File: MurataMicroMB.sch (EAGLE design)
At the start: 47 parts, among them CON1 C-2395.MurataMicroSD, CON3 CON_MIL_10_ARM, CON4 C-2395.microSD, IC1 74LVC1G00DBV, IC2 IC_DCDC_LM27313, IC3 IC_LPC11U3XQFN33, IC4 IC_LDO_XX1117_4, Q1 CLOCK_CRYSTAL_4_3225, SW1 SW_TACTSW_2PP8073, SW2 SW_TACTSW_2PP8073, SW3 SW_TACTSW_2PP8073, X1 TSW-102-02-S-S

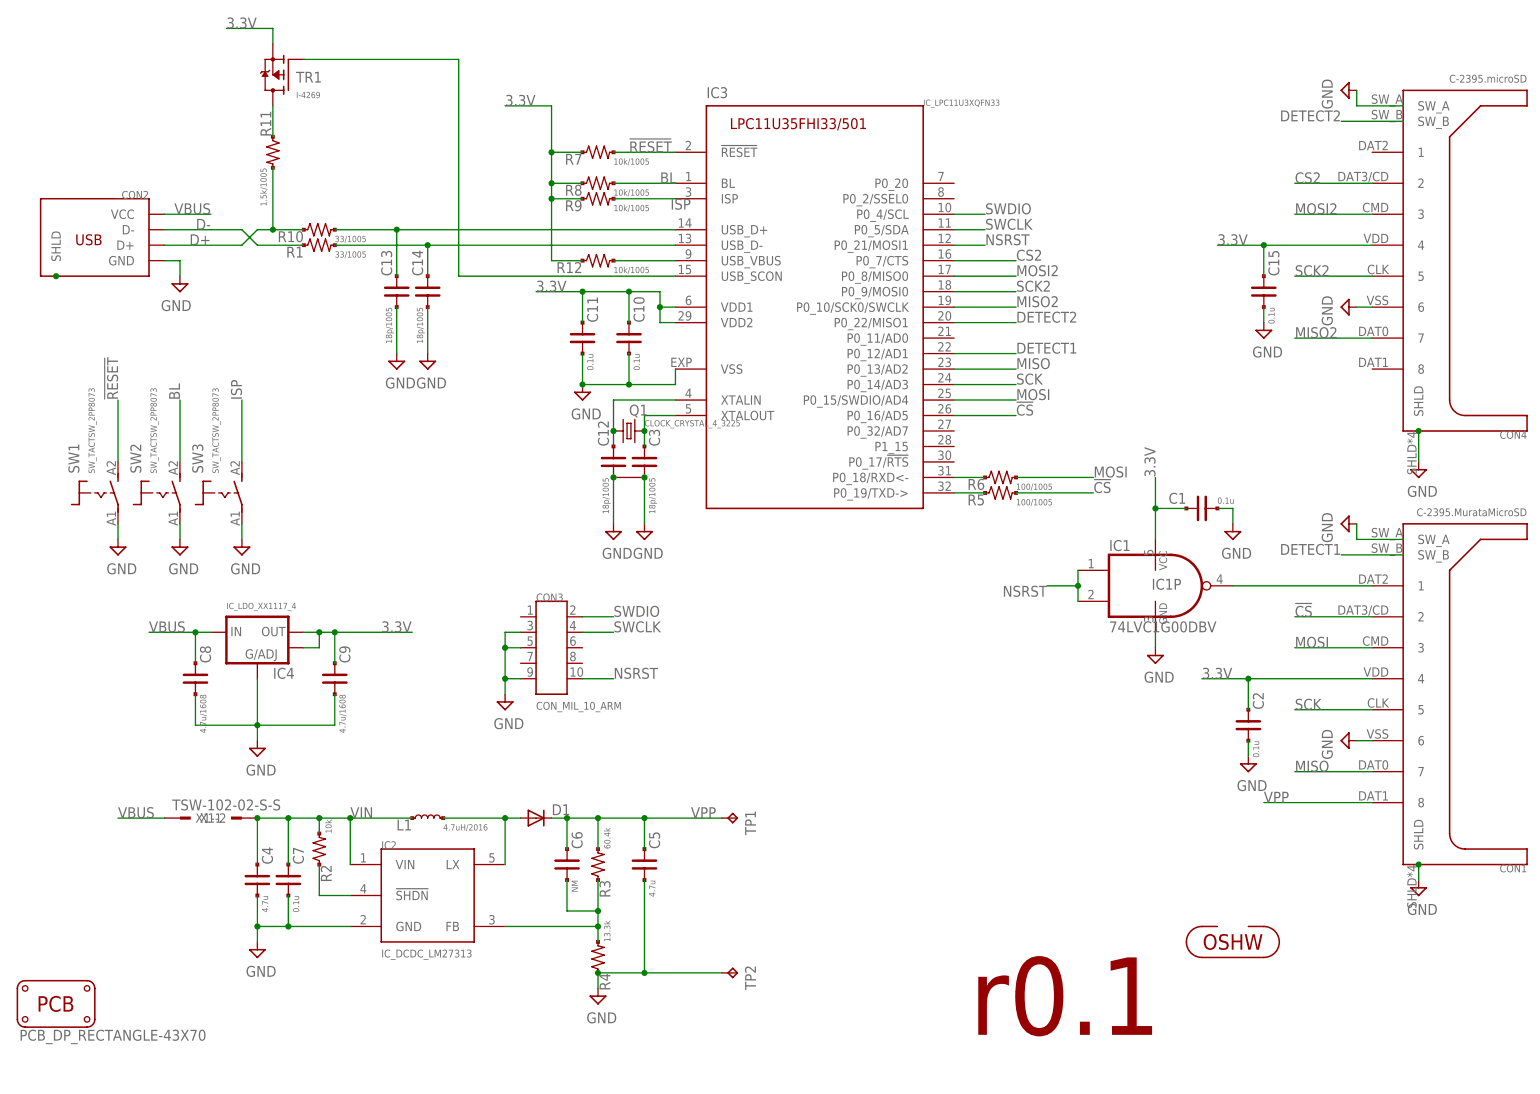
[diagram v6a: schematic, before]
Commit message: [ MB ] add LED1/R13/R14
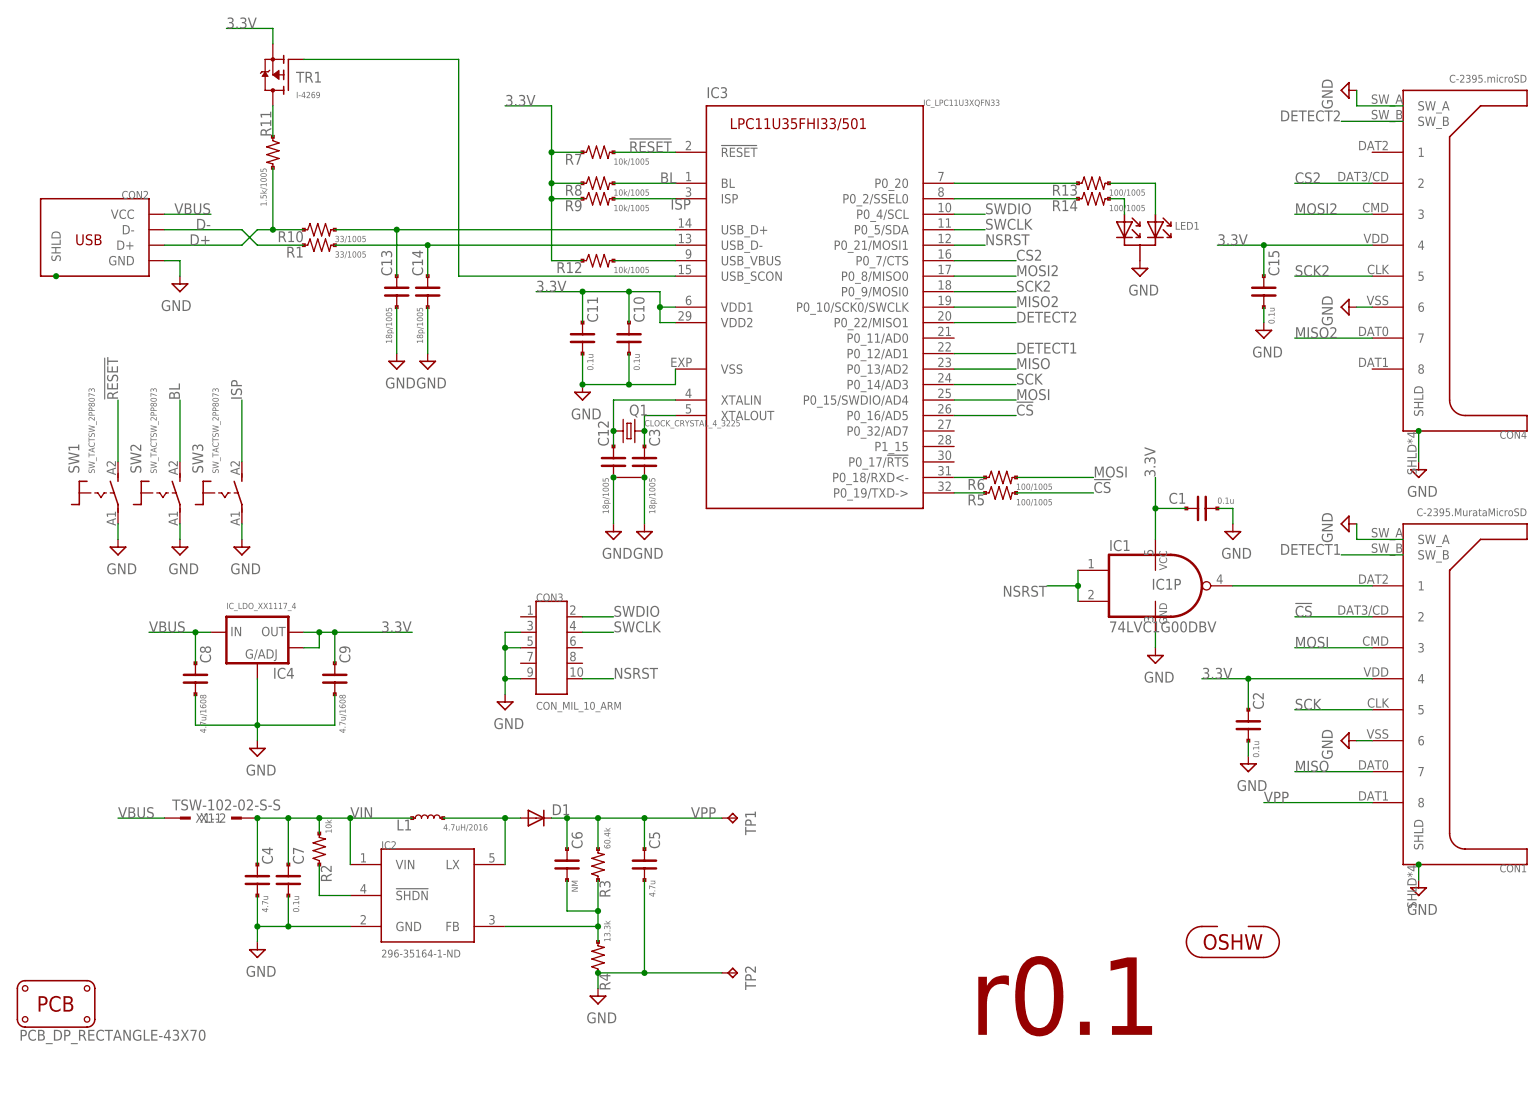
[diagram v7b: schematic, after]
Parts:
- added LED1: (no value), mylib:LED_1SEG_A2K1
- added R13, R14: 100/1005, mylib:R_US_PAD_PAD_1005
- IC2: value IC_DCDC_LM27313 -> 296-35164-1-ND
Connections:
- new net N$1: IC3.P0_2/SSEL0, R14.1
- new net N$14: IC3.P0_20, R13.1
- new net N$15: LED1.A2, R13.2
- new net N$16: LED1.A1, R14.2
- net GND: now also LED1.K1
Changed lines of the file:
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@@
 <part name="SUPPLY8" library="mylib" deviceset="GND" device=""/>
 <part name="L1" library="mylib" deviceset="INDUCTOR" device="_2016" value="4.7uH/2016"/>
-<part name="IC2" library="mylib" deviceset="IC_DCDC_LM27313" device=""/>
+<part name="IC2" library="mylib" deviceset="IC_DCDC_LM27313" device="" value="296-35164-1-ND"/>
 <part name="D1" library="mylib" deviceset="DIODE_SMALL" device=""/>
 <part name="R2" library="mylib" deviceset="R_US_PAD_PAD" device="_1608" value="10k"/>
@@
 <part name="SUPPLY22" library="mylib" deviceset="GND" device=""/>
 <part name="SUPPLY23" library="mylib" deviceset="GND" device=""/>
+<part name="R13" library="mylib" deviceset="R_US_PAD_PAD" device="_1005" value="100/1005"/>
+<part name="R14" library="mylib" deviceset="R_US_PAD_PAD" device="_1005" value="100/1005"/>
+<part name="LED1" library="mylib" deviceset="LED_1SEG_A2K1" device=""/>
+<part name="SUPPLY24" library="mylib" deviceset="GND" device=""/>
 </parts>
 <sheets>
@@
 <instance part="SUPPLY22" gate="GND" x="223.52" y="160.02" rot="R270"/>
 <instance part="SUPPLY23" gate="GND" x="223.52" y="88.9" rot="R270"/>
+<instance part="R13" gate="G$1" x="182.88" y="144.78"/>
+<instance part="R14" gate="G$1" x="182.88" y="142.24"/>
+<instance part="LED1" gate="G$1" x="190.5" y="137.16"/>
+<instance part="SUPPLY24" gate="GND" x="190.5" y="129.54"/>
 </instances>
 <busses>
@@
 <wire x1="226.06" y1="88.9" x2="226.06" y2="86.36" width="0.1524" layer="91"/>
 <wire x1="226.06" y1="86.36" x2="233.68" y2="86.36" width="0.1524" layer="91"/>
+</segment>
+<segment>
+<pinref part="LED1" gate="G$1" pin="K1"/>
+<pinref part="SUPPLY24" gate="GND" pin="GND"/>
 </segment>
 </net>
@@
 </segment>
 </net>
+<net name="N$1" class="0">
+<segment>
+<pinref part="R14" gate="G$1" pin="1"/>
+<pinref part="IC3" gate="G$1" pin="P0_2/SSEL0"/>
+<wire x1="180.34" y1="142.24" x2="160.02" y2="142.24" width="0.1524" layer="91"/>
+</segment>
+</net>
+<net name="N$14" class="0">
+<segment>
+<pinref part="IC3" gate="G$1" pin="P0_20"/>
+<pinref part="R13" gate="G$1" pin="1"/>
+<wire x1="160.02" y1="144.78" x2="180.34" y2="144.78" width="0.1524" layer="91"/>
+</segment>
+</net>
+<net name="N$15" class="0">
+<segment>
+<pinref part="R13" gate="G$1" pin="2"/>
+<pinref part="LED1" gate="G$1" pin="A2"/>
+<wire x1="185.42" y1="144.78" x2="193.04" y2="144.78" width="0.1524" layer="91"/>
+<wire x1="193.04" y1="144.78" x2="193.04" y2="139.7" width="0.1524" layer="91"/>
+</segment>
+</net>
+<net name="N$16" class="0">
+<segment>
+<pinref part="R14" gate="G$1" pin="2"/>
+<pinref part="LED1" gate="G$1" pin="A1"/>
+<wire x1="185.42" y1="142.24" x2="187.96" y2="142.24" width="0.1524" layer="91"/>
+<wire x1="187.96" y1="142.24" x2="187.96" y2="139.7" width="0.1524" layer="91"/>
+</segment>
+</net>

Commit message: [ MB ][ SCH ] values and details change
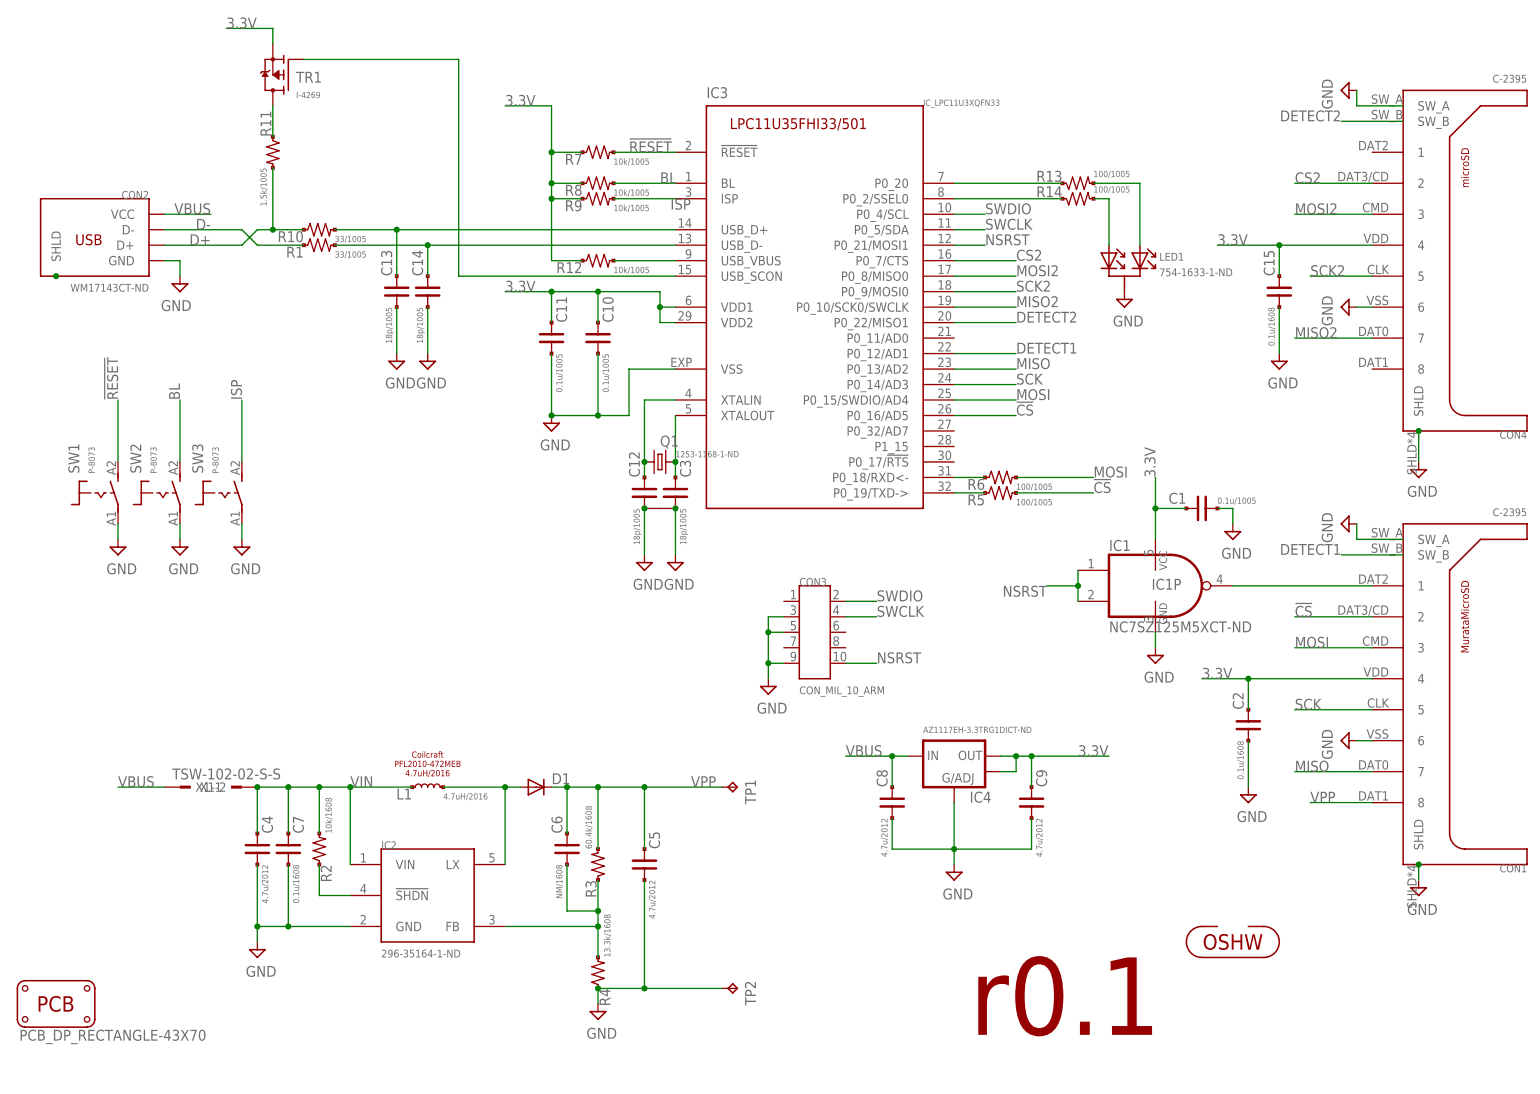
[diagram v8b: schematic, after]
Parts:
- C1, C10, C11: value 0.1u -> 0.1u/1005
- C15, C2, C7: value 0.1u -> 0.1u/1608
- C4, C5: value 4.7u -> 4.7u/2012
- C6: value NM -> NM/1608
- C8, C9: value 4.7u/1608 -> 4.7u/2012
- CON1: value C-2395.MurataMicroSD -> C-2395
- CON2: value (none) -> WM17143CT-ND
- CON4: value C-2395.microSD -> C-2395
- IC1: value 74LVC1G00DBV -> NC7SZ125M5XCT-ND
- IC4: value IC_LDO_XX1117_4 -> AZ1117EH-3.3TRG1DICT-ND
- LED1: value (none) -> 754-1633-1-ND
- Q1: value CLOCK_CRYSTAL_4_3225 -> 1253-1168-1-ND
- R2: value 10k -> 10k/1608
- R3: value 60.4k -> 60.4k/1608
- R4: value 13.3k -> 13.3k/1608
- SW1, SW2, SW3: value SW_TACTSW_2PP8073 -> P-8073
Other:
- note added: "Coilcraft PFL2010-472MEB 4.7uH/2016"
- note added: "MurataMicroSD"
- note added: "microSD"
- moved on the sheet: C10, C11, C12, C15, C3, C4, C6, C7, C8, C9, CON3, D1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
